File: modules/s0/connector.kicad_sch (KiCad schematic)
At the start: 5 parts, among them J1 P8, J2 P9, J7 Conn_01x02, J8 Conn_01x02, U1 BEAGLEBONEBLACK

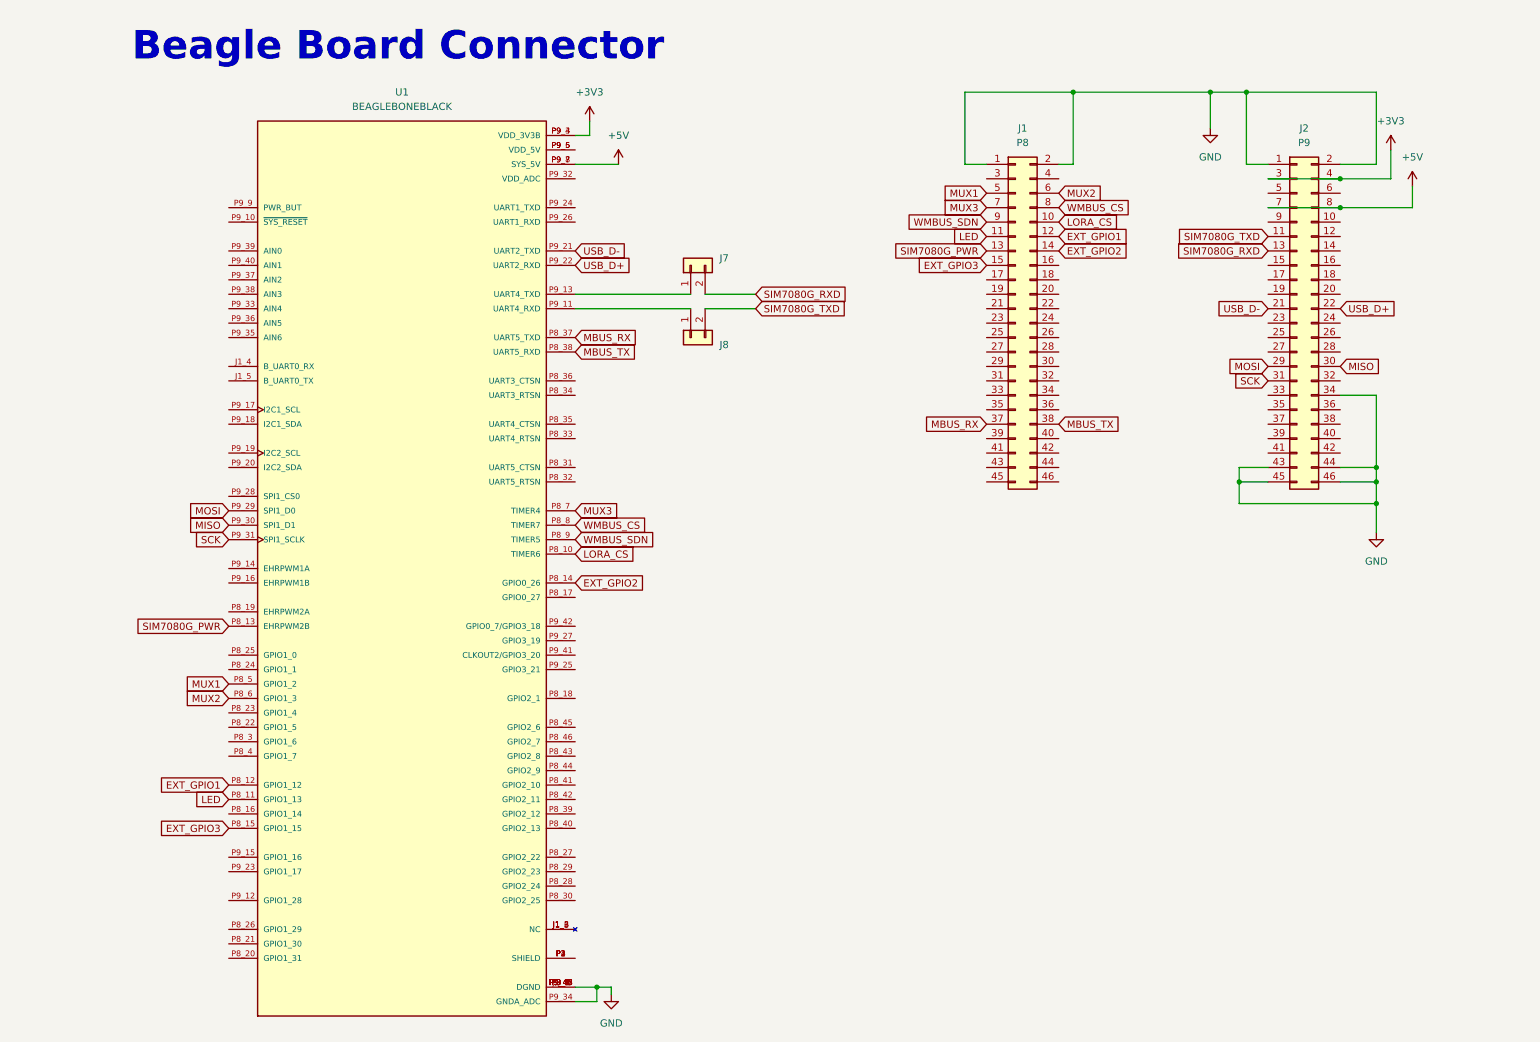
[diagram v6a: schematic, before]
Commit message: feat(s0): migrate from c3 to c6
Signed-off-by: Rodney Osodo <socials@rodneyosodo.com>
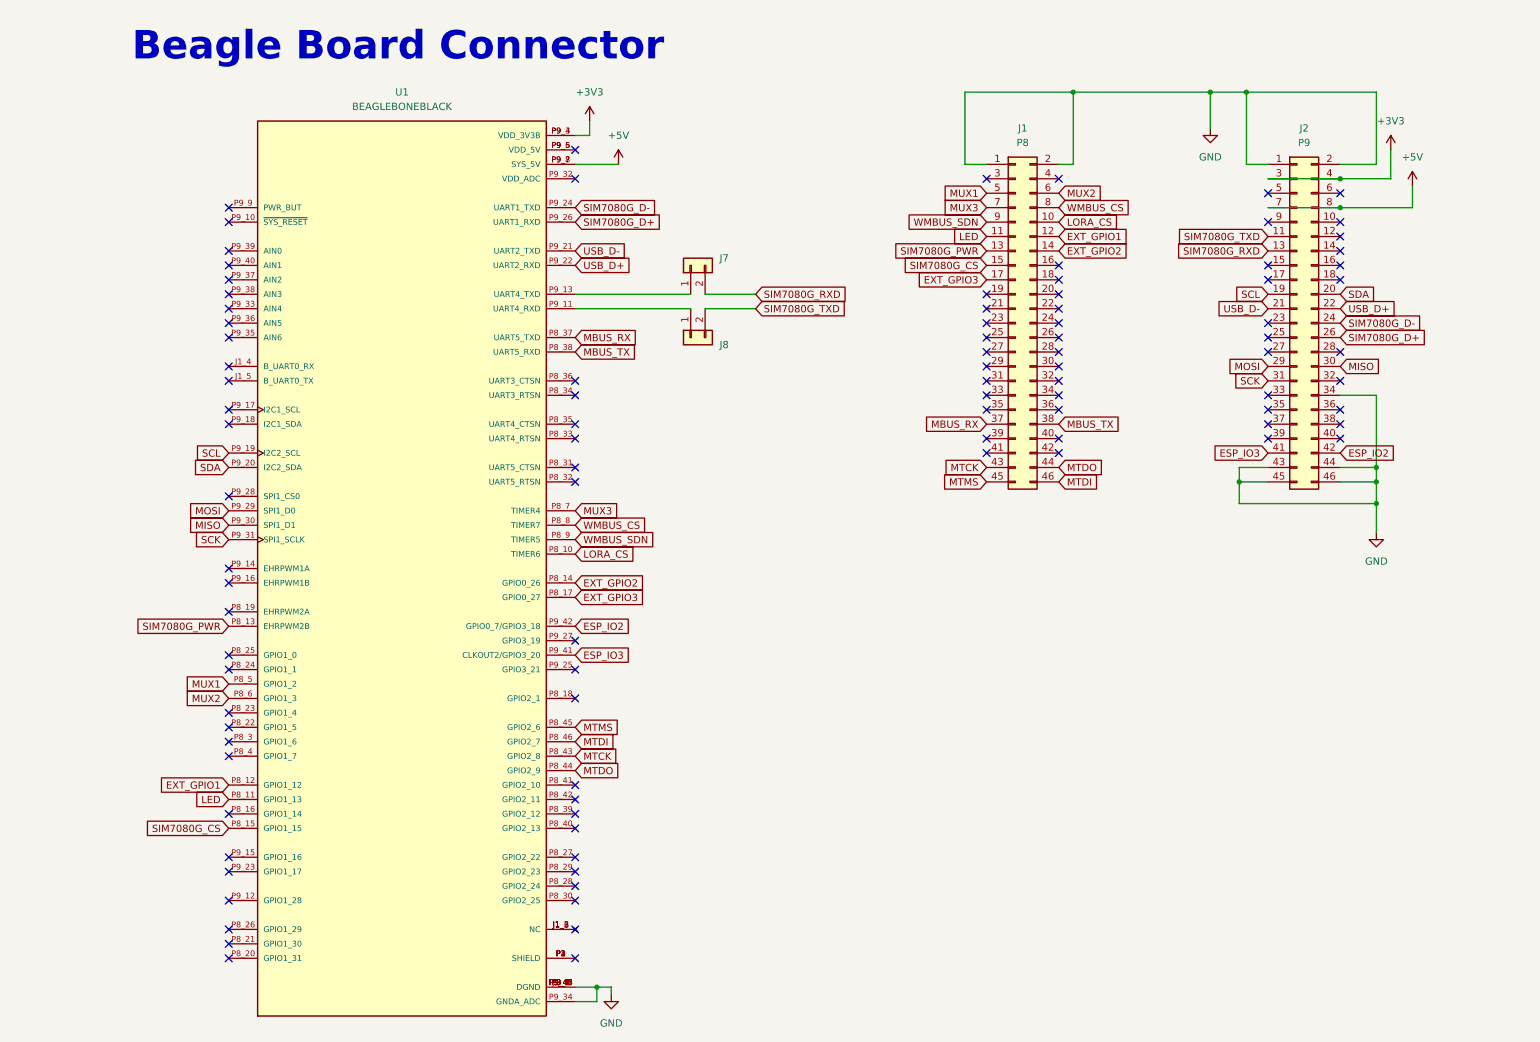
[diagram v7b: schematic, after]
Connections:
- net EXT_GPIO3: now also J1.17 (Pin_17), U1.P8_17 (GPIO0_27); no longer J1.15 (Pin_15), U1.P8_15 (GPIO1_15)
- net MTCK: now reaches U1.P8_43 (GPIO2_8)
- net MTCK: now also J1.43 (Pin_43)
- net MTDO: now reaches U1.P8_44 (GPIO2_9)
- net MTDO: now also J1.44 (Pin_44)
- net MTMS: now reaches U1.P8_45 (GPIO2_6)
- net MTMS: now also J1.45 (Pin_45)
- net MTDI: now reaches U1.P8_46 (GPIO2_7)
- net MTDI: now also J1.46 (Pin_46)
- net SCL: now reaches U1.P9_19 (I2C2_SCL)
- net SCL: now also J2.19 (Pin_19)
- net SDA: now reaches U1.P9_20 (I2C2_SDA)
- net SDA: now also J2.20 (Pin_20)
- net SIM7080G_D-: now reaches U1.P9_24 (UART1_TXD)
- net SIM7080G_D-: now also J2.24 (Pin_24)
- net SIM7080G_D+: now reaches U1.P9_26 (UART1_RXD)
- net SIM7080G_D+: now also J2.26 (Pin_26)
- net ESP_IO3: now reaches U1.P9_41 (CLKOUT2/GPIO3_20)
- net ESP_IO3: now also J2.41 (Pin_41)
- net ESP_IO2: now reaches U1.P9_42 (GPIO0_7/GPIO3_18)
- net ESP_IO2: now also J2.42 (Pin_42)
- new net SIM7080G_CS: J1.15 (Pin_15), U1.P8_15 (GPIO1_15)
- no-connect marks 0 -> 99

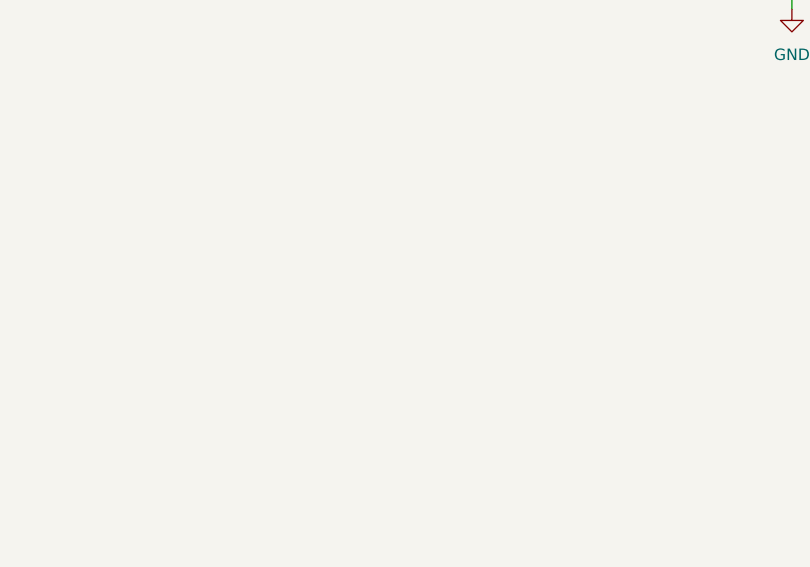
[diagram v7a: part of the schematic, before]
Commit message: fix(s0): add UART header
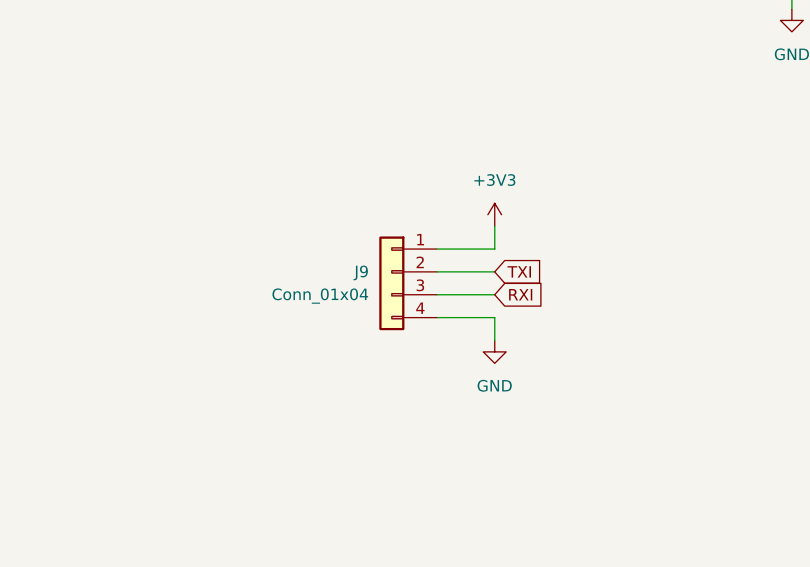
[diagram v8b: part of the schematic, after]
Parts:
- added J9: Conn_01x04, Connector_PinHeader_2.54mm:PinHeader_1x04_P2.54mm_Vertical, symbol Connector_Generic:Conn_01x04
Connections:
- net +3V3: now also J9.1 (Pin_1)
- net GND: now also J9.4 (Pin_4)
- new net RXI: J9.3 (Pin_3)
- new net TXI: J9.2 (Pin_2)
